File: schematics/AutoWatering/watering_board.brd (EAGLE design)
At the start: 50.8 x 55.5 mm, 9 parts, among them IC2 REG1117, Q1 NMOSFET, Q2 NMOSFET

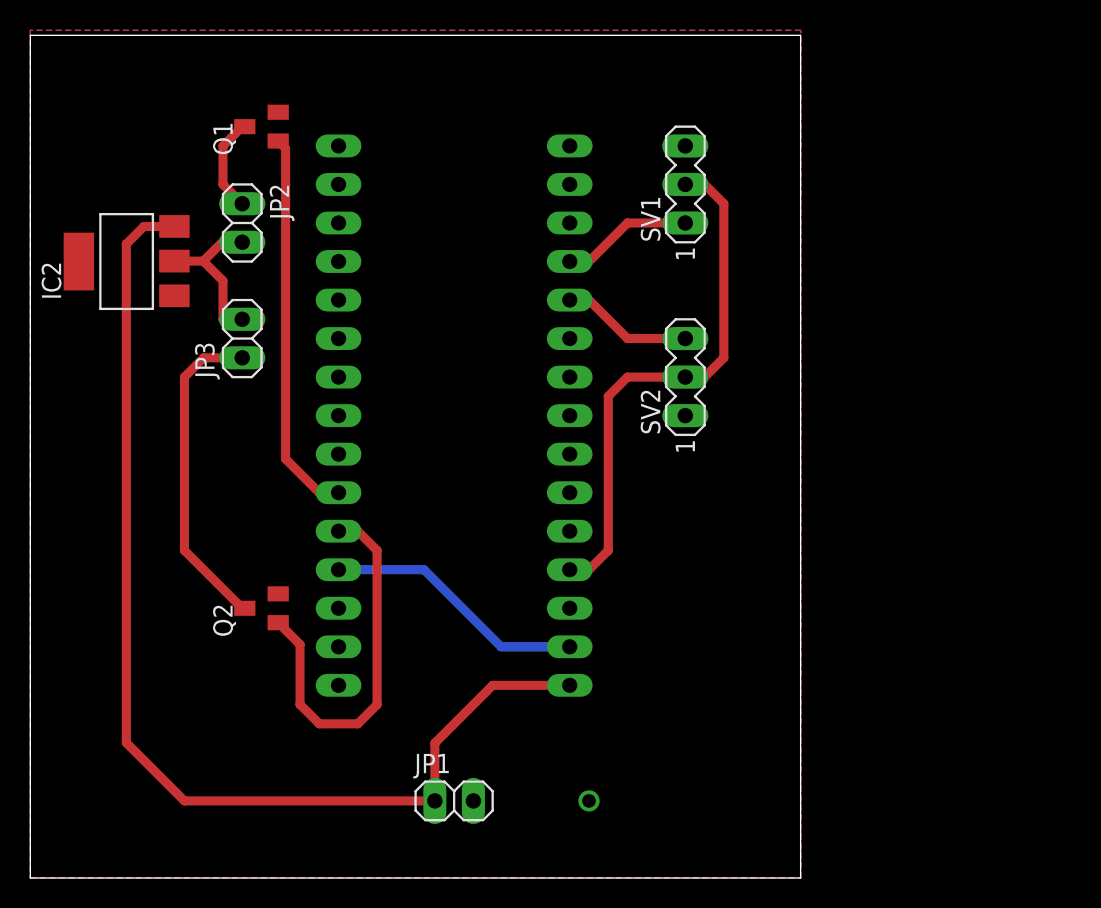
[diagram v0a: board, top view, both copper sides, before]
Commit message: Add missing LSO capacitors
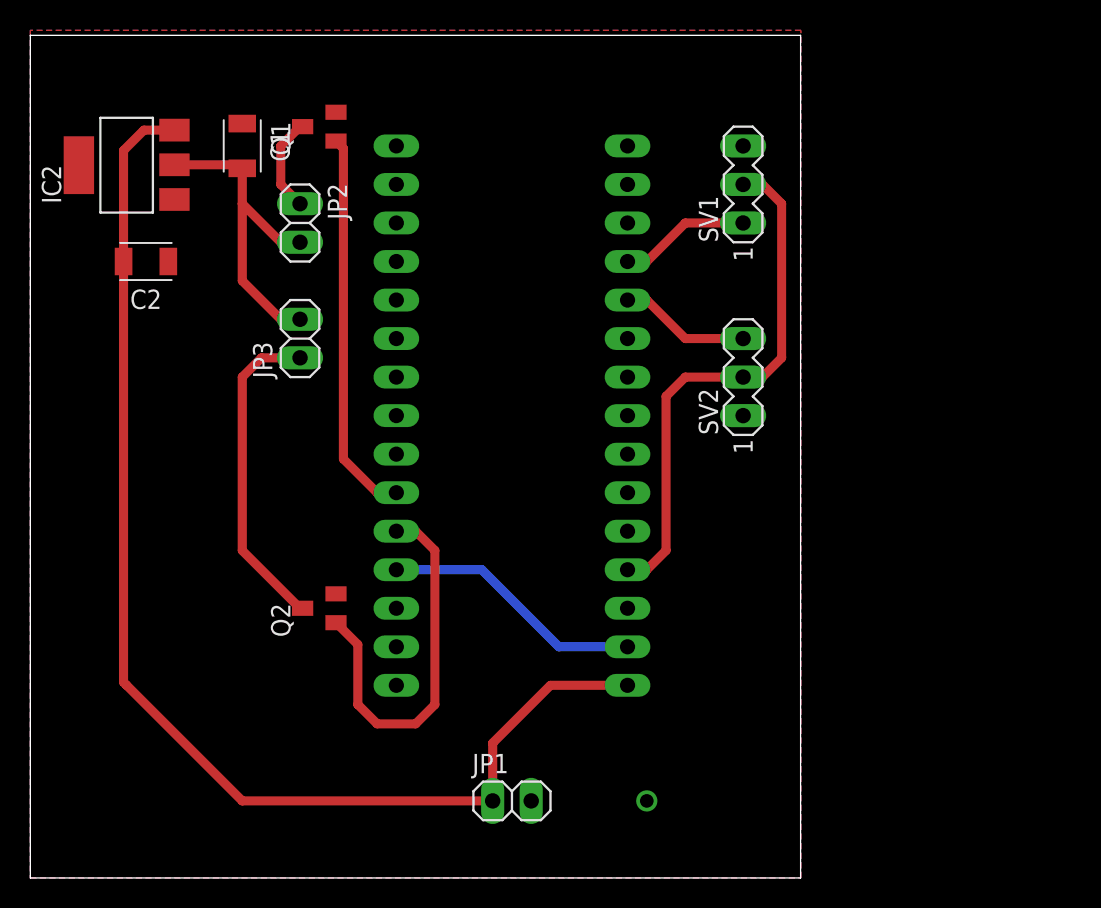
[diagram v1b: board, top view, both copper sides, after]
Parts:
- added C1: 100u, Capacitor:CAPC3216X135
- added C2: 10u, Capacitor:CAPC3216X135
- moved IC2 6.35 mm to (6.35, 47.0)
- moved SV1 3.81 mm to (47.0, 45.7)
- moved SV2 3.81 mm to (47.0, 33.0)
- moved JP2 3.81 mm to (17.8, 43.2)
- moved JP3 3.81 mm to (17.8, 35.6)
- moved Q1 3.81 mm to (19.1, 49.5)
- moved Q2 3.81 mm to (19.1, 17.8)
- moved JP1 3.81 mm to (31.8, 5.08)
- moved U$1 3.81 mm to (31.8, 30.5)
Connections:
- net GND: now also C1.1, C2.1
- net N$4: now also C2.2
- net N$9: now also C1.2
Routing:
- net N$9: track 10.7 -> 21.7 mm
- net N$4: track 72.7 -> 80.8 mm

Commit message: Use USB A conntector for the pump
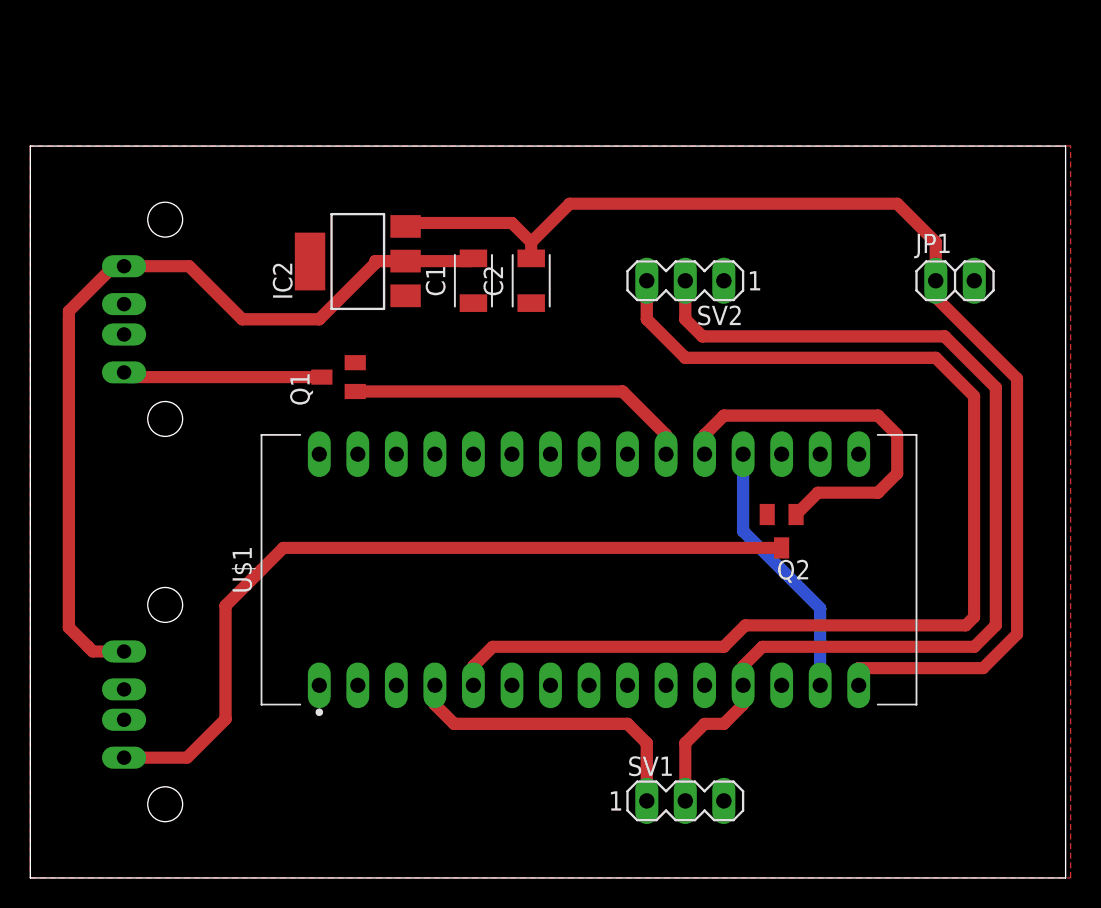
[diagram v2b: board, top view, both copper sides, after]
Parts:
- removed JP2, JP3: (no value), pinhead:1X02
- added X1, X2: (no value), con-berg:PN87520
- moved JP1 45.0 mm to (61.0, 39.4)
- moved SV1 40.8 mm to (43.2, 5.08), turned to 0 degrees
- moved Q2 30.9 mm to (49.5, 22.9), turned to 180 degrees
- moved C2 25.4 mm to (33.0, 39.4), turned to 90 degrees
- moved C1 17.6 mm to (29.2, 39.4), turned to 90 degrees
- moved Q1 16.6 mm to (20.3, 33.0)
- moved IC2 16.5 mm to (21.6, 40.6)
- moved U$1 11.4 mm to (36.8, 20.3), flipped to the top, turned to 90 degrees
- moved SV2 7.41 mm to (43.2, 39.4), turned to 180 degrees
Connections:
- net N$6: now also X1.4; no longer JP2.1
- net N$7: now also X2.4; no longer JP3.1
- net N$9: now also X1.1, X2.1; no longer JP2.2, JP3.2
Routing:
- net N$2: track 8.67 -> 76.4 mm
- net N$9: track 21.7 -> 56.9 mm
- net N$3: track 35.1 -> 69.5 mm
- net N$7: track 21.3 -> 53.5 mm
- net N$1: track 8.67 -> 20.1 mm
- net N$6: track 6.30 -> 13.2 mm
- net N$8: track 25.6 -> 22.9 mm
- net N$4: track 80.8 -> 79.3 mm
- net GND: vias 1 -> 0
- removed copper zone on layer 16, net GND
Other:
- board size 50.8 x 55.5 mm -> 68.2 x 48.2 mm

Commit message: Add the case
Add the case for the schematics.
Update to Arduino every. Use the difference sleep/wakeup mechnism.
Adjust moisture sensors.
Update schematics to match the case.
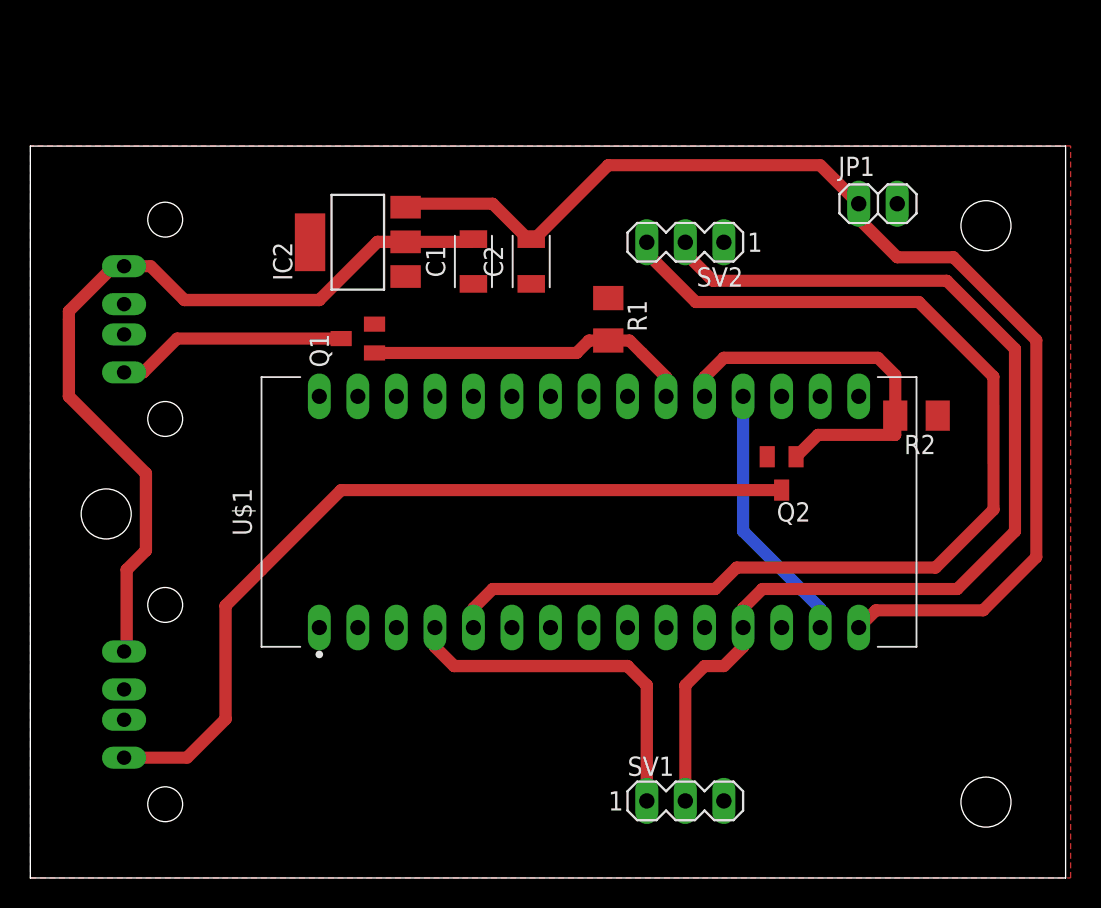
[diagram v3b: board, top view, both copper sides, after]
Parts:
- added R1, R2: (no value), rcl:M1206
- moved JP1 7.18 mm to (55.9, 44.5)
- moved Q2 3.81 mm to (49.5, 26.7)
- moved U$1 3.81 mm to (36.8, 24.1)
- moved Q1 2.84 mm to (21.6, 35.6)
- moved SV2 2.54 mm to (43.2, 41.9)
- moved C1 1.27 mm to (29.2, 40.6)
- moved C2 1.27 mm to (33.0, 40.6)
- moved IC2 1.27 mm to (21.6, 41.9)
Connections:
- net GND: now also R1.1, R2.1
- net N$5: now also R2.2
- net N$8: now also R1.2
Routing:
- net N$1: track 20.1 -> 23.9 mm
- net N$3: track 69.5 -> 72.1 mm
- net N$2: track 76.4 -> 74.0 mm
- net N$6: track 13.2 -> 15.2 mm
- net N$7: track 53.5 -> 55.0 mm
- net N$9: track 56.9 -> 55.6 mm
- net N$8: track 22.9 -> 21.8 mm
- net N$4: track 79.3 -> 78.2 mm
- net N$5: track 25.4 -> 25.9 mm
